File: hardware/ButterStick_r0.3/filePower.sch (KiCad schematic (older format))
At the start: 71 parts, among them J6 JST_PA, U1 TLV725P, U15 TPS542951, U21 LTC4367, U22 AON7804, U8 TLV718P, U9 XCL206B123CR-G

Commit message: hw.r0_3: Experiment with buses
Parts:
- removed C73: 4.7uF, pkl_dipol:C_0603, symbol Device:C
- removed C74: 10uF, pkl_dipol:C_0603, symbol Device:C
- removed U9: XCL206B123CR-G, gkl_housings_dfn:CL-2025, symbol gkl_pmic:XCL206
- C10, C15, C16, C17, C18, C19, C20, C21, C22, C23, C3, C4, C48, C49, C51, C57, C58, C59, C6, C60, C61, C62, C63, C64, C65, C66, C7, C75, C76, C77, C78, C79, C8, C9, C92, C96, C97, C98, C99: footprint pkl_dipol:C_0402 -> Capacitor_SMD:C_0402_1005Metric
- C11, C13, C14, C68: footprint pkl_dipol:C_0603 -> Capacitor_SMD:C_0603_1608Metric
- C52, C53, C54, C56, C67, C69, C70: footprint pkl_dipol:C_0805 -> Capacitor_SMD:C_0805_2012Metric
- R43, R44, R45, R46, R56, R57, R58, R59, R61, R62: footprint pkl_dipol:R_0402 -> Resistor_SMD:R_0402_1005Metric

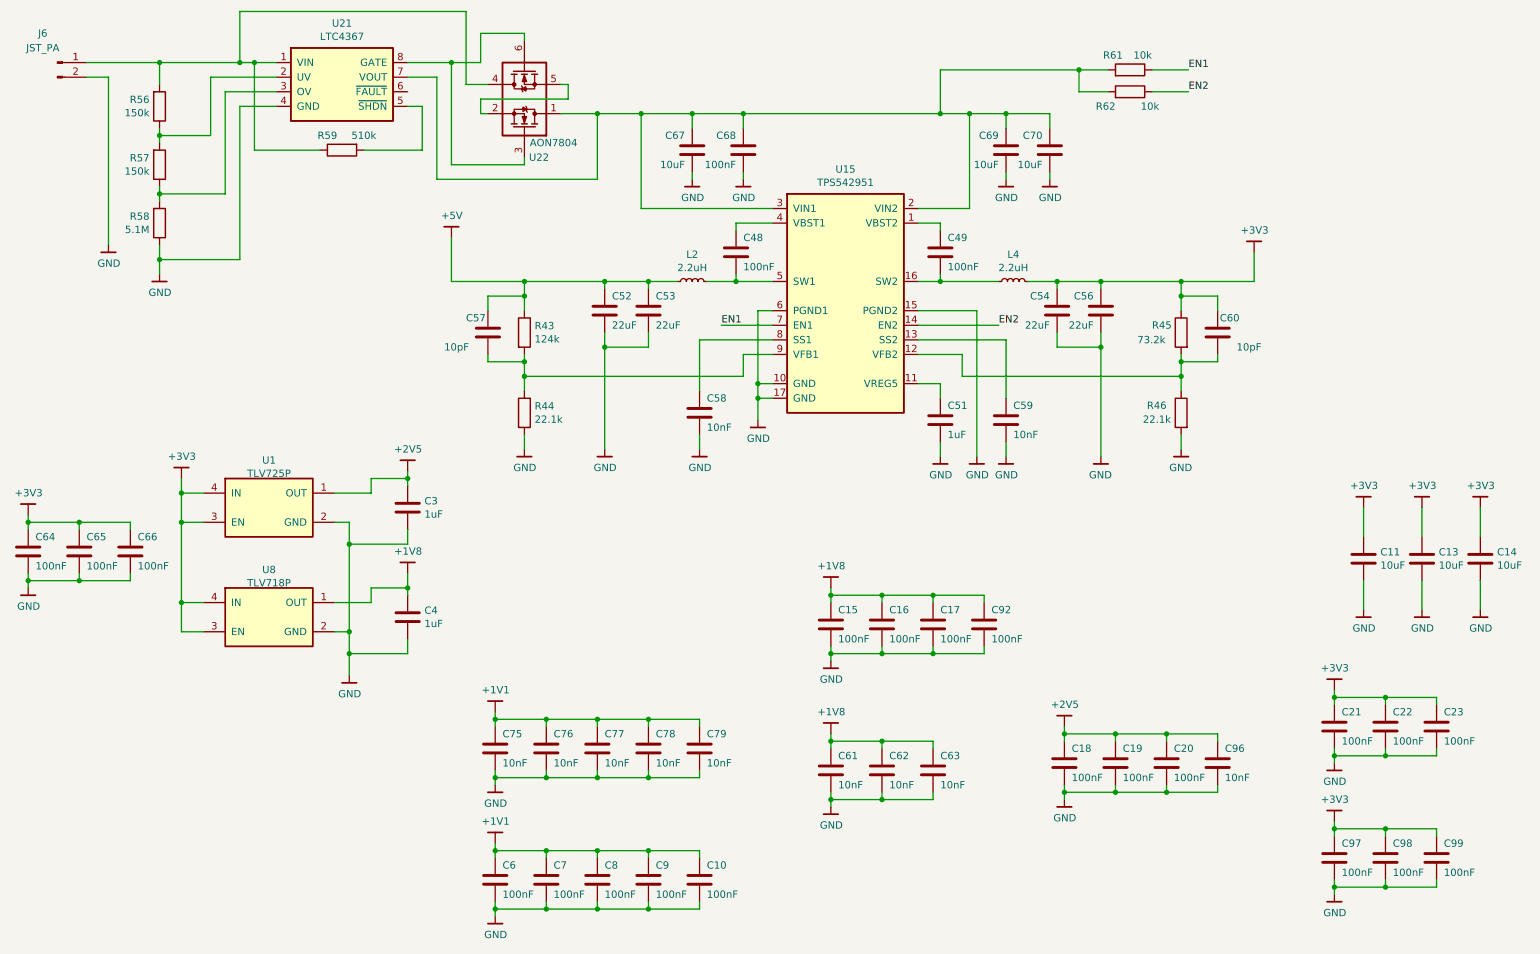
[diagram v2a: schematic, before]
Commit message: hw.r0_3: Update schematics with 85F-5G symbol
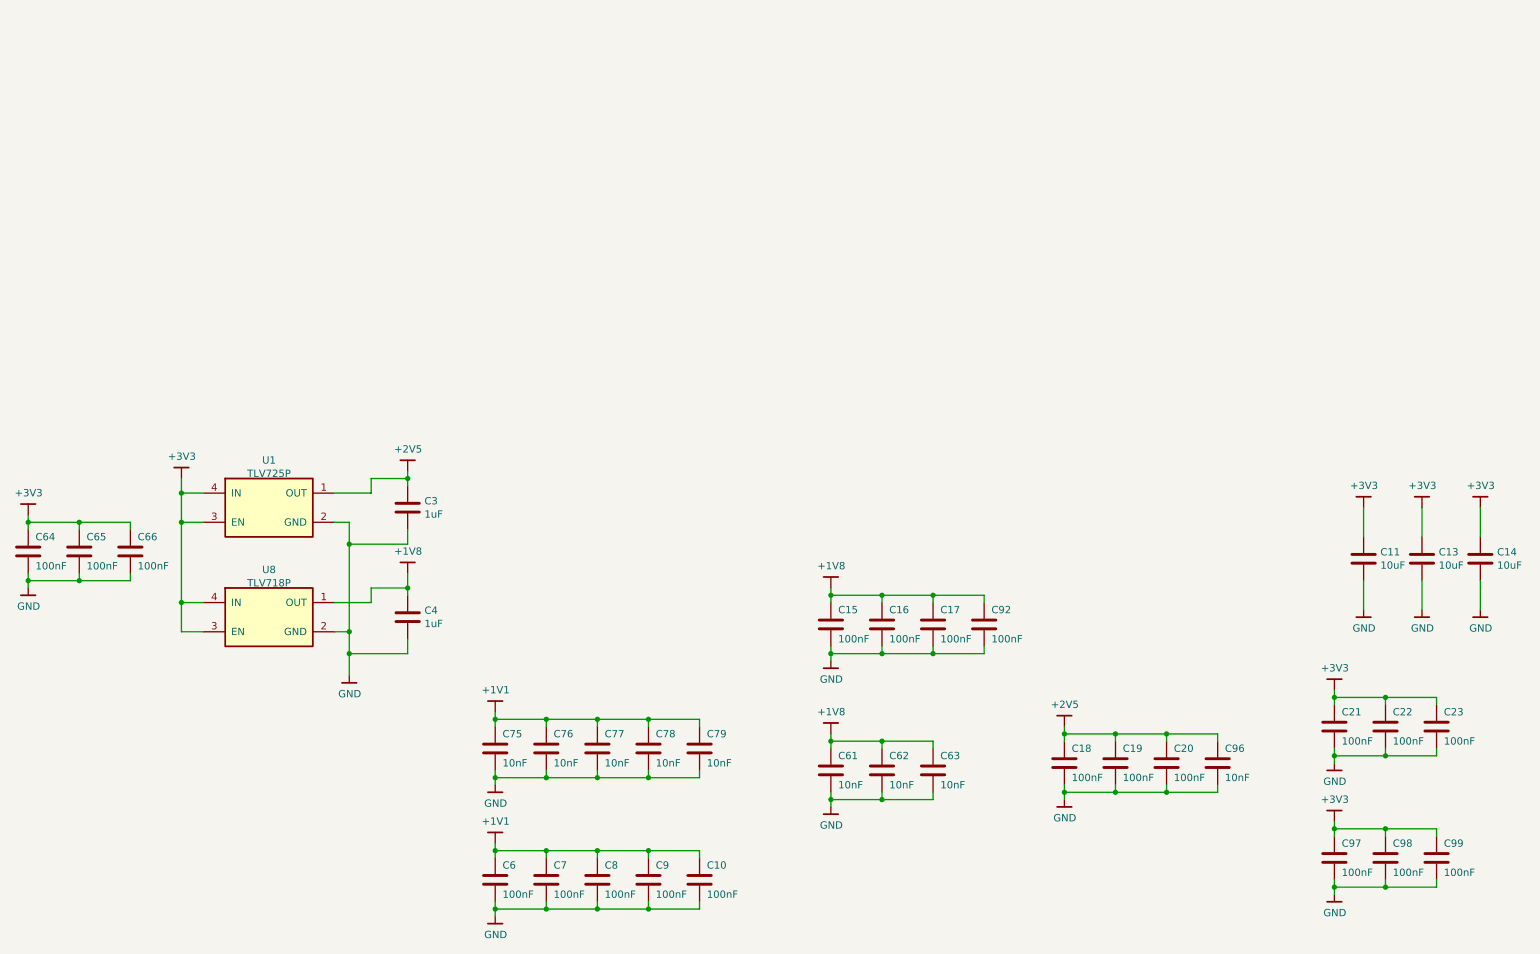
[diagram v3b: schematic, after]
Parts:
- removed C48, C49: 100nF, Capacitor_SMD:C_0402_1005Metric, symbol Device:C
- removed C51: 1uF, Capacitor_SMD:C_0402_1005Metric, symbol Device:C
- removed C52, C53, C54, C56: 22uF, Capacitor_SMD:C_0805_2012Metric, symbol Device:C
- removed C57, C60: 10pF, Capacitor_SMD:C_0402_1005Metric, symbol Device:C
- removed C58, C59: 10nF, Capacitor_SMD:C_0402_1005Metric, symbol Device:C
- removed C67, C69, C70: 10uF, Capacitor_SMD:C_0805_2012Metric, symbol Device:C
- removed C68: 100nF, Capacitor_SMD:C_0603_1608Metric, symbol Device:C
- removed J6: JST_PA, gkl_conn:SB02B-PASK-2, symbol Connector:Conn_01x02_Male
- removed L2, L4: 2.2uH, Inductor_SMD:L_Taiyo-Yuden_MD-5050, symbol Device:L_Small
- removed R43: 124k, Resistor_SMD:R_0402_1005Metric, symbol Device:R
- removed R44, R46: 22.1k, Resistor_SMD:R_0402_1005Metric, symbol Device:R
- removed R45: 73.2k, Resistor_SMD:R_0402_1005Metric, symbol Device:R
- removed R56, R57: 150k, Resistor_SMD:R_0402_1005Metric, symbol Device:R
- removed R58: 5.1M, Resistor_SMD:R_0402_1005Metric, symbol Device:R
- removed R59: 510k, Resistor_SMD:R_0402_1005Metric, symbol Device:R
- removed R61, R62: 10k, Resistor_SMD:R_0402_1005Metric, symbol Device:R
- removed U15: TPS542951, Package_DFN_QFN:QFN-16-1EP_4x4mm_P0.65mm_EP2.7x2.7mm_ThermalVias, symbol gkl_pmic:TPS542951
- removed U21: LTC4367, Package_SO:MSOP-8_3x3mm_P0.65mm, symbol gkl_pmic:LTC4367
- removed U22: AON7804, gkl_housings_dfn:DFN3X3_8L_EP2_P, symbol gkl_mosfet:AON7804
